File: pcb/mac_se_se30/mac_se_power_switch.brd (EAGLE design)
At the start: 27.1 x 59 mm, 7 parts, among them J1 POWER_JACKPTH

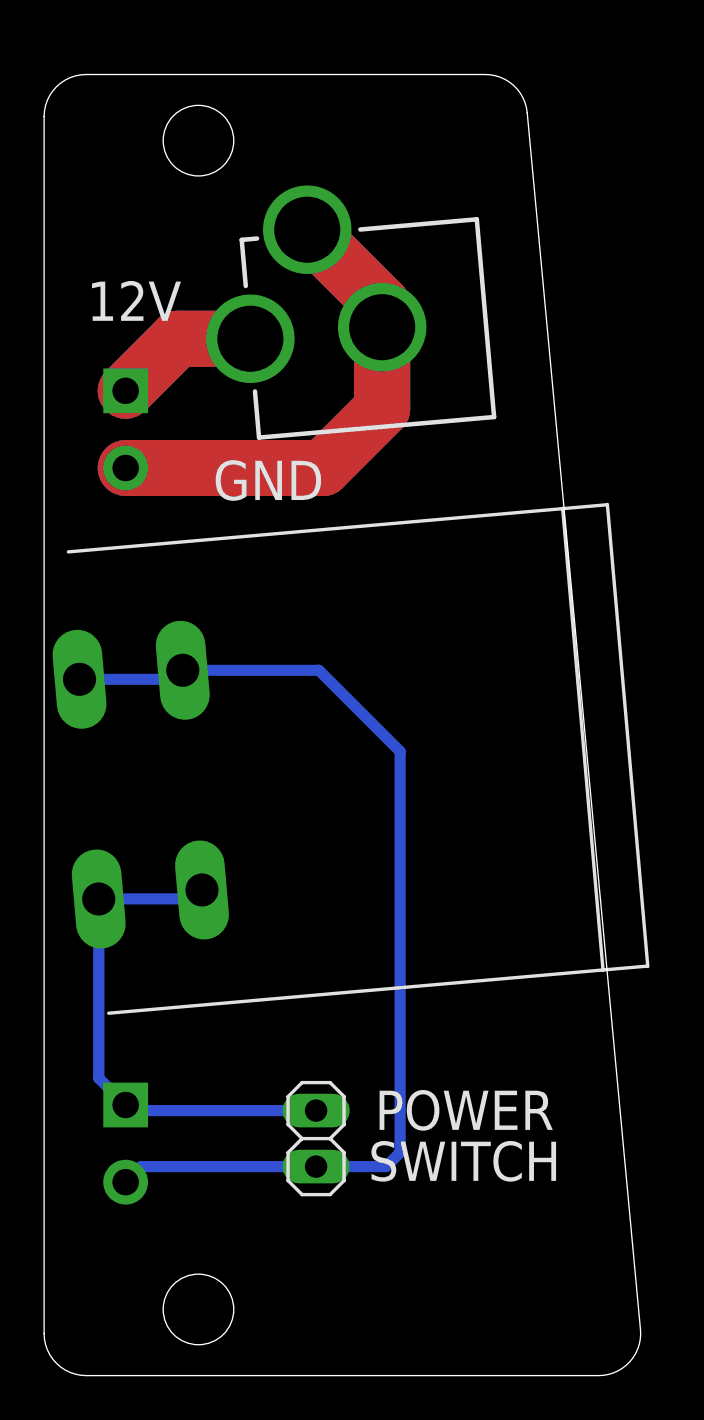
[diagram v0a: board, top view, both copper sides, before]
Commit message: updating mac SE atx adaptor
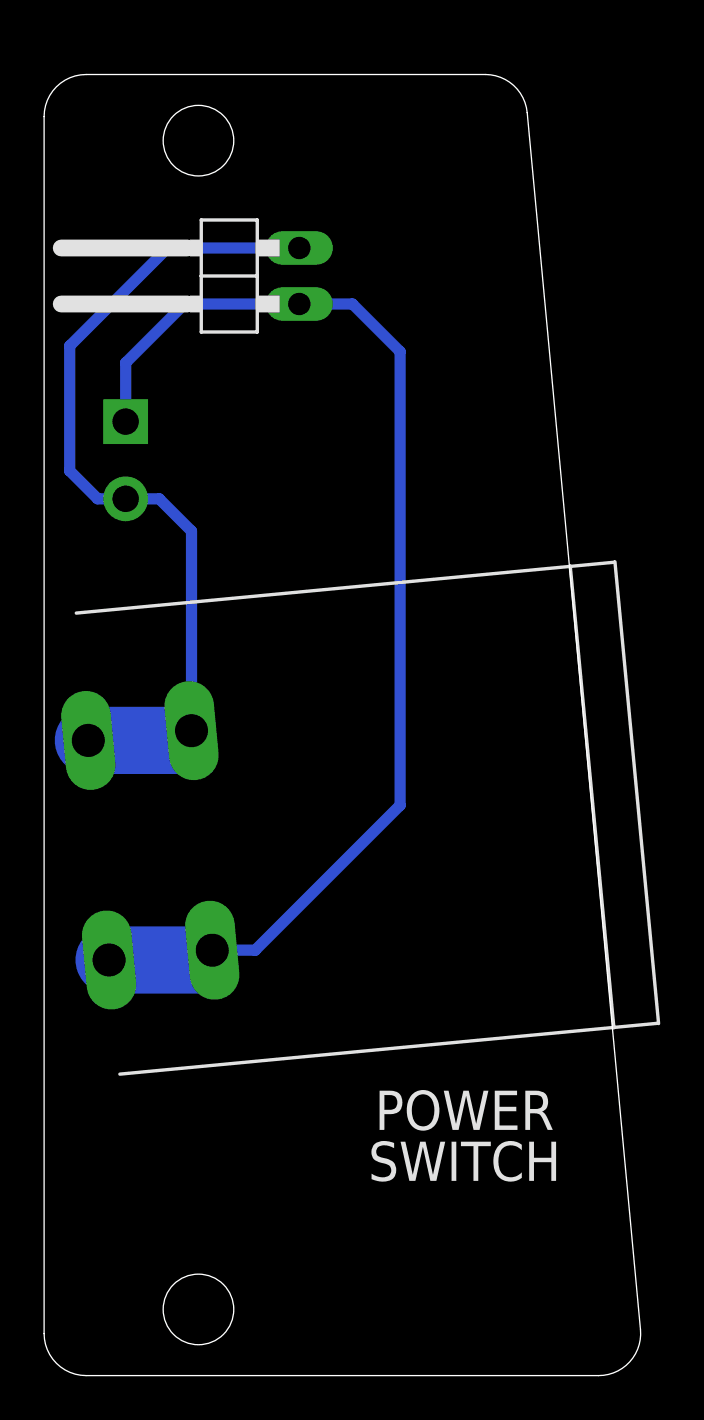
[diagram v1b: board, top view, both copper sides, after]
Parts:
- removed J1: POWER_JACKPTH, SparkFun:POWER_JACK_PTH
- removed J2: (no value), atx_power_control:SCREWTERMINAL-3.5MM-2-NS
- JP2: device pinhead:1X02 -> pinhead:1X02/90
- moved JP2 39.4 mm to (0.76, 46.9), turned to 90 degrees
- moved J7 31.0 mm to (-3.30, 40.3)
- moved U$1 2.80 mm to (-4.55, 21.1), turned to 275.4 degrees
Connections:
- removed net N$1: J1.GND, J1.GNDBREAK, J2.2
- removed net N$4: J1.PWR, J2.1
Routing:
- net N$1: track 44.5 -> 0.00 mm
- net N$3: track 23.4 -> 53.8 mm
- net N$4: track 13.3 -> 0.00 mm
- net N$2: track 47.4 -> 38.5 mm
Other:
- board text added: "PT1 dekuNukem Nov 2022"
- board text removed: "12V"
- board text removed: "GND"
- board text removed: "PT0 dekuNukem Nov 2022"
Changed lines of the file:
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@@
 <wire x1="20.0442375" y1="-0.918428125" x2="14.906890625" y2="54.27156875" width="0" layer="20"/>
 <wire x1="14.906890625" y1="54.27156875" x2="13.010090625" y2="56" width="0" layer="20" curve="84.681981"/>
-<text x="10.541" y="1.397" size="1.778" layer="26" distance="35" rot="MR180" align="center">Instructions:
+<text x="11.303" y="0.635" size="1.778" layer="26" distance="35" rot="MR180" align="center">Instructions:
 atx4vc.com</text>
 <text x="10.541" y="25.273" size="1.778" layer="26" distance="35" rot="MR90" align="center">Macintosh SE ATX
 Power Board</text>
-<text x="4.318" y="24.765" size="1.4224" layer="26" distance="30" rot="MR90" align="center">PT0 dekuNukem
+<text x="4.318" y="24.765" size="1.4224" layer="26" distance="30" rot="MR90" align="center">PT1 dekuNukem
 Nov 2022</text>
 <wire x1="14.7334" y1="56.8706" x2="20.3722" y2="-3.8862" width="0.1524" layer="51"/>
-<text x="3.175" y="37.592" size="1.778" layer="25" distance="30" rot="R180" align="center">GND</text>
-<text x="-2.921" y="45.72" size="1.778" layer="25" distance="30" rot="R180" align="center">12V</text>
 <text x="12.065" y="7.874" size="1.778" layer="25" distance="30" rot="R180" align="center">POWER
 SWITCH</text>
@@
 </autorouter>
 <elements>
-<element name="J7" library="atx_power_control" package="SCREWTERMINAL-3.5MM-2-NS" value="" x="-3.302" y="9.271" smashed="yes" rot="R270">
-<attribute name="PROD_ID" value="CONN-13512" x="-3.302" y="9.271" size="1.778" layer="27" rot="R270" display="off"/>
-<attribute name="SF_ID" value="PRT-09918" x="-3.302" y="9.271" size="1.778" layer="27" rot="R270" display="off"/>
-<attribute name="SF_SKU" value="PRT-08432" x="-3.302" y="9.271" size="1.778" layer="27" rot="R270" display="off"/>
-<attribute name="SKU" value="PRT-09914" x="-3.302" y="9.271" size="1.778" layer="27" rot="R270" display="off"/>
-<attribute name="VALUE" x="-2.032" y="10.541" size="0.6096" layer="27" font="vector" ratio="20" rot="R270"/>
+<element name="J7" library="atx_power_control" package="SCREWTERMINAL-3.5MM-2-NS" value="" x="-3.302" y="40.259" smashed="yes" rot="R270">
+<attribute name="PROD_ID" value="CONN-13512" x="-3.302" y="40.259" size="1.778" layer="27" rot="R270" display="off"/>
+<attribute name="SF_ID" value="PRT-09918" x="-3.302" y="40.259" size="1.778" layer="27" rot="R270" display="off"/>
+<attribute name="SF_SKU" value="PRT-08432" x="-3.302" y="40.259" size="1.778" layer="27" rot="R270" display="off"/>
+<attribute name="SKU" value="PRT-09914" x="-3.302" y="40.259" size="1.778" layer="27" rot="R270" display="off"/>
+<attribute name="VALUE" x="-2.032" y="41.529" size="0.6096" layer="27" font="vector" ratio="20" rot="R270"/>
 </element>
-<element name="JP2" library="pinhead" library_urn="urn:adsk.eagle:library:325" package="1X02" package3d_urn="urn:adsk.eagle:package:22435/2" value="" x="5.334" y="7.747" smashed="yes" rot="R270">
-<attribute name="POPULARITY" value="98" x="5.334" y="7.747" size="1.778" layer="27" rot="R270" display="off"/>
-<attribute name="VALUE" x="2.159" y="10.287" size="1.27" layer="27" rot="R270"/>
+<element name="JP2" library="pinhead" library_urn="urn:adsk.eagle:library:325" package="1X02/90" package3d_urn="urn:adsk.eagle:package:22437/2" value="" x="0.762" y="46.863" smashed="yes" rot="R90">
+<attribute name="POPULARITY" value="24" x="0.762" y="46.863" size="1.778" layer="27" rot="R90" display="off"/>
+<attribute name="VALUE" x="3.937" y="44.323" size="1.27" layer="27" rot="R90"/>
 </element>
 <element name="U$2" library="a" package="M3_MOUNTING_HOLE_PACK" value="M3_MOUNTING_HOLE" x="0" y="0" smashed="yes"/>
 <element name="U$3" library="a" package="M3_MOUNTING_HOLE_PACK" value="M3_MOUNTING_HOLE" x="0" y="53" smashed="yes"/>
-<element name="U$1" library="atx4vc" package="ROCK_SWITCH" value="ROCK_SW" x="-4.984" y="23.892" smashed="yes" rot="R275"/>
-<element name="J1" library="SparkFun" package="POWER_JACK_PTH" value="POWER_JACKPTH" x="16.002" y="45.212" smashed="yes" rot="R95"/>
-<element name="J2" library="atx_power_control" package="SCREWTERMINAL-3.5MM-2-NS" value="" x="-3.302" y="41.656" smashed="yes" rot="R270">
-<attribute name="PROD_ID" value="CONN-13512" x="-3.302" y="41.656" size="1.778" layer="27" rot="R270" display="off"/>
-<attribute name="SF_ID" value="PRT-09918" x="-3.302" y="41.656" size="1.778" layer="27" rot="R270" display="off"/>
-<attribute name="SF_SKU" value="PRT-08432" x="-3.302" y="41.656" size="1.778" layer="27" rot="R270" display="off"/>
-<attribute name="SKU" value="PRT-09914" x="-3.302" y="41.656" size="1.778" layer="27" rot="R270" display="off"/>
-<attribute name="VALUE" x="-2.032" y="42.926" size="0.6096" layer="27" font="vector" ratio="20" rot="R270"/>
-</element>
+<element name="U$1" library="atx4vc" package="ROCK_SWITCH" value="ROCK_SW" x="-4.5522" y="21.1234" smashed="yes" rot="R275.4"/>
 </elements>
 <signals>
@@
 <contactref element="J7" pad="2"/>
 <contactref element="JP2" pad="2"/>
-<wire x1="-5.39363125" y1="28.5741125" x2="-1.12115" y2="28.5741125" width="0.508" layer="16"/>
-<wire x1="-1.12115" y1="28.5741125" x2="-0.711515625" y2="28.983746875" width="0.508" layer="16"/>
-<wire x1="-0.711515625" y1="28.983746875" x2="5.460253125" y2="28.983746875" width="0.508" layer="16"/>
-<wire x1="8.509" y1="6.477" x2="5.334" y2="6.477" width="0.508" layer="16"/>
-<wire x1="9.144" y1="7.112" x2="8.509" y2="6.477" width="0.508" layer="16"/>
-<wire x1="9.144" y1="25.3" x2="9.144" y2="7.112" width="0.508" layer="16"/>
-<wire x1="5.460253125" y1="28.983746875" x2="9.144" y2="25.3" width="0.508" layer="16"/>
-<wire x1="-3.302" y1="5.771" x2="-2.596" y2="6.477" width="0.508" layer="16"/>
-<wire x1="-2.596" y1="6.477" x2="5.334" y2="6.477" width="0.508" layer="16"/>
+<wire x1="-4.99450625" y1="25.802540625" x2="-0.68935" y2="25.8055125" width="3.048" layer="16"/>
+<wire x1="-0.68935" y1="25.8055125" x2="-0.315365625" y2="26.24485" width="0.508" layer="16"/>
+<wire x1="-0.315365625" y1="35.296365625" x2="-1.778" y2="36.759" width="0.508" layer="16"/>
+<wire x1="-3.302" y1="36.759" x2="-1.778" y2="36.759" width="0.508" layer="16"/>
+<wire x1="-0.315365625" y1="35.296365625" x2="-0.315365625" y2="26.24485" width="0.508" layer="16"/>
+<wire x1="-3.302" y1="36.759" x2="-4.572" y2="36.759" width="0.508" layer="16"/>
+<wire x1="-4.572" y1="36.759" x2="-5.842" y2="38.029" width="0.508" layer="16"/>
+<wire x1="-5.842" y1="38.029" x2="-5.842" y2="43.688" width="0.508" layer="16"/>
+<wire x1="-5.842" y1="43.688" x2="-1.397" y2="48.133" width="0.508" layer="16"/>
+<wire x1="-1.397" y1="48.133" x2="4.572" y2="48.133" width="0.508" layer="16"/>
 </signal>
 <signal name="N$3">
@@
 <contactref element="J7" pad="1"/>
 <contactref element="JP2" pad="1"/>
-<wire x1="5.334" y1="9.017" x2="-3.048" y2="9.017" width="0.508" layer="16"/>
-<wire x1="-3.048" y1="9.017" x2="-3.302" y2="9.271" width="0.508" layer="16"/>
-<wire x1="-3.302" y1="9.271" x2="-4.522071875" y2="10.491071875" width="0.508" layer="16"/>
-<wire x1="-4.522071875" y1="10.491071875" x2="-4.522071875" y2="18.612165625" width="0.508" layer="16"/>
-<wire x1="-4.522071875" y1="18.612165625" x2="-0.249596875" y2="18.612165625" width="0.508" layer="16"/>
-<wire x1="-0.249596875" y1="18.612165625" x2="0.1600375" y2="19.0218" width="0.508" layer="16"/>
-</signal>
-<signal name="N$1">
-<contactref element="J1" pad="GNDBREAK"/>
-<contactref element="J1" pad="GND"/>
-<contactref element="J2" pad="2"/>
-<wire x1="4.933084375" y1="48.961546875" x2="8.3313" y2="45.56333125" width="2.54" layer="16"/>
-<wire x1="8.3313" y1="45.56333125" x2="8.3313" y2="44.5409" width="2.54" layer="16"/>
-<wire x1="8.3313" y1="44.5409" x2="8.3313" y2="40.8433" width="2.54" layer="16"/>
-<wire x1="5.644" y1="38.156" x2="-3.302" y2="38.156" width="2.54" layer="16"/>
-<wire x1="8.3313" y1="40.8433" x2="5.644" y2="38.156" width="2.54" layer="16"/>
-<wire x1="4.933084375" y1="48.961546875" x2="8.3313" y2="45.56333125" width="2.54" layer="1"/>
-<wire x1="8.3313" y1="45.56333125" x2="8.3313" y2="44.5409" width="2.54" layer="1"/>
-<wire x1="8.3313" y1="44.5409" x2="8.3313" y2="40.8433" width="2.54" layer="1"/>
-<wire x1="5.644" y1="38.156" x2="-3.302" y2="38.156" width="2.54" layer="1"/>
-<wire x1="8.3313" y1="40.8433" x2="5.644" y2="38.156" width="2.54" layer="1"/>
-</signal>
-<signal name="N$4">
-<contactref element="J1" pad="PWR"/>
-<contactref element="J2" pad="1"/>
-<wire x1="-3.302" y1="41.656" x2="-0.940034375" y2="44.017965625" width="2.54" layer="16"/>
-<wire x1="-0.940034375" y1="44.017965625" x2="2.354134375" y2="44.017965625" width="2.54" layer="16"/>
-<wire x1="2.354134375" y1="44.017965625" x2="-0.940034375" y2="44.017965625" width="2.54" layer="1"/>
-<wire x1="-0.940034375" y1="44.017965625" x2="-3.302" y2="41.656" width="2.54" layer="1"/>
+<wire x1="-4.053425" y1="15.84691875" x2="0.182203125" y2="15.843565625" width="3.048" layer="16"/>
+<wire x1="0.182203125" y1="15.843565625" x2="0.6257125" y2="16.289228125" width="0.508" layer="16"/>
+<wire x1="2.573228125" y1="16.289228125" x2="0.6257125" y2="16.289228125" width="0.508" layer="16"/>
+<wire x1="9.144" y1="22.86" x2="2.573228125" y2="16.289228125" width="0.508" layer="16"/>
+<wire x1="-3.302" y1="40.259" x2="-3.302" y2="42.926" width="0.508" layer="16"/>
+<wire x1="-0.635" y1="45.593" x2="4.572" y2="45.593" width="0.508" layer="16"/>
+<wire x1="-3.302" y1="42.926" x2="-0.635" y2="45.593" width="0.508" layer="16"/>
+<wire x1="4.572" y1="45.593" x2="6.985" y2="45.593" width="0.508" layer="16"/>
+<wire x1="6.985" y1="45.593" x2="9.144" y2="43.434" width="0.508" layer="16"/>
+<wire x1="9.144" y1="43.434" x2="9.144" y2="22.86" width="0.508" layer="16"/>
 </signal>
 </signals>

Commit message: updated mac SE pcb
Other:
- board text added: "Macintosh SE ATX Power Switch"
- board text removed: "Macintosh SE ATX Power Board"
- board text removed: "POWER SWITCH"
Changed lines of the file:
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@@
 <wire x1="20.0442375" y1="-0.918428125" x2="14.906890625" y2="54.27156875" width="0" layer="20"/>
 <wire x1="14.906890625" y1="54.27156875" x2="13.010090625" y2="56" width="0" layer="20" curve="84.681981"/>
-<text x="11.303" y="0.635" size="1.778" layer="26" distance="35" rot="MR180" align="center">Instructions:
+<text x="8.763" y="7.493" size="1.778" layer="25" distance="35" rot="R180" align="center">Instructions:
 atx4vc.com</text>
-<text x="10.541" y="25.273" size="1.778" layer="26" distance="35" rot="MR90" align="center">Macintosh SE ATX
-Power Board</text>
-<text x="4.318" y="24.765" size="1.4224" layer="26" distance="30" rot="MR90" align="center">PT1 dekuNukem
+<text x="11.303" y="44.577" size="1.778" layer="25" distance="35" rot="R270" align="center">Macintosh SE ATX
+Power Switch</text>
+<text x="10.541" y="1.27" size="1.4224" layer="25" distance="30" align="center">PT1 dekuNukem
 Nov 2022</text>
 <wire x1="14.7334" y1="56.8706" x2="20.3722" y2="-3.8862" width="0.1524" layer="51"/>
-<text x="12.065" y="7.874" size="1.778" layer="25" distance="30" rot="R180" align="center">POWER
-SWITCH</text>
 </plain>
 <attributes>

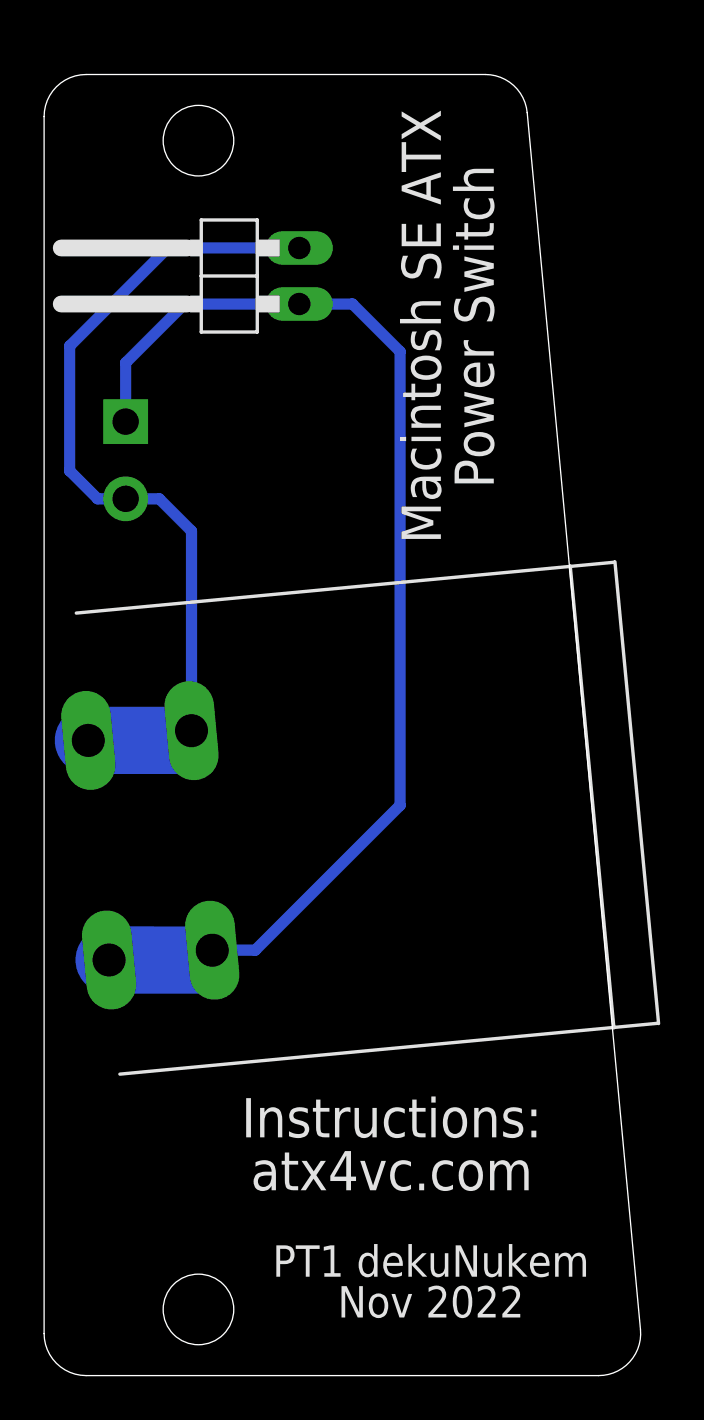
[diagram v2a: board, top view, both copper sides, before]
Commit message: updated switch footprint
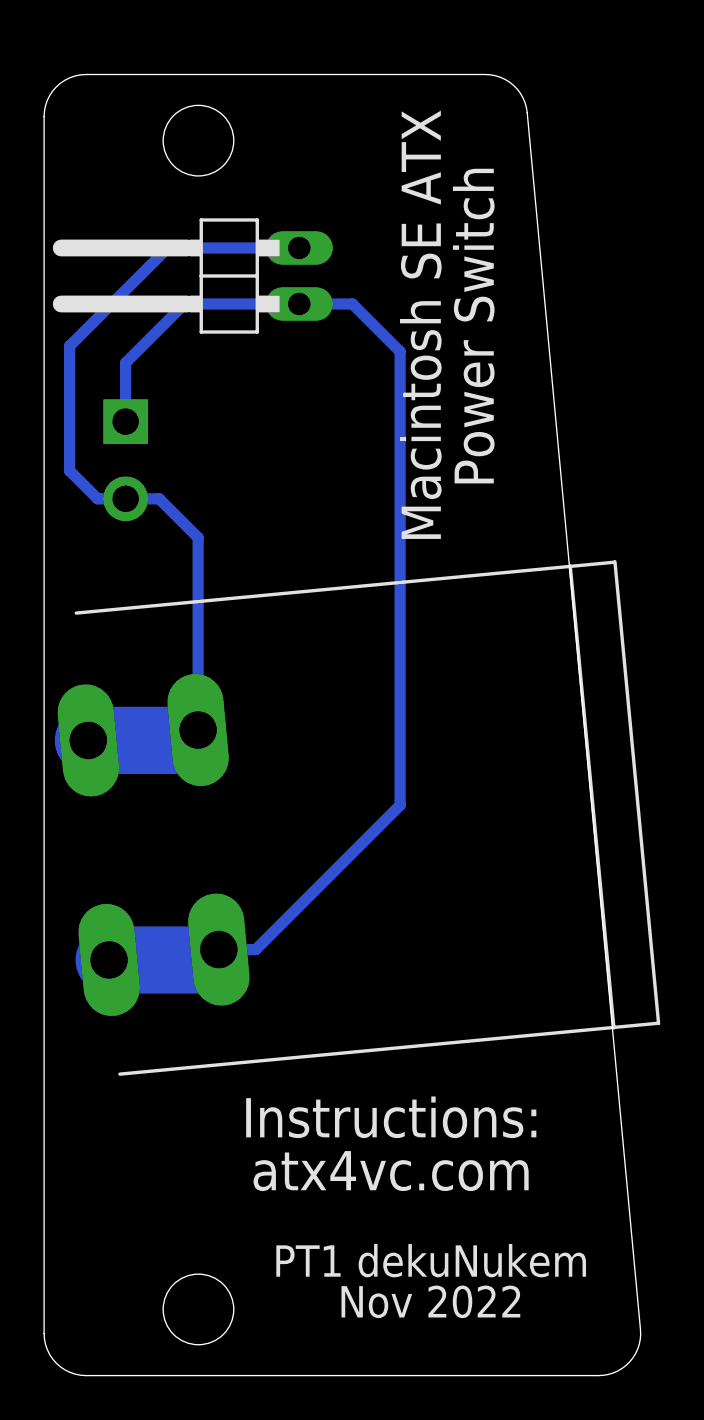
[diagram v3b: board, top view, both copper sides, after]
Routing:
- net N$3: track 53.8 -> 52.9 mm
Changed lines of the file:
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@@
 <contactref element="JP2" pad="2"/>
 <wire x1="-4.99450625" y1="25.802540625" x2="-0.68935" y2="25.8055125" width="3.048" layer="16"/>
-<wire x1="-0.68935" y1="25.8055125" x2="-0.315365625" y2="26.24485" width="0.508" layer="16"/>
-<wire x1="-0.315365625" y1="35.296365625" x2="-1.778" y2="36.759" width="0.508" layer="16"/>
 <wire x1="-3.302" y1="36.759" x2="-1.778" y2="36.759" width="0.508" layer="16"/>
-<wire x1="-0.315365625" y1="35.296365625" x2="-0.315365625" y2="26.24485" width="0.508" layer="16"/>
 <wire x1="-3.302" y1="36.759" x2="-4.572" y2="36.759" width="0.508" layer="16"/>
 <wire x1="-4.572" y1="36.759" x2="-5.842" y2="38.029" width="0.508" layer="16"/>
@@
 <wire x1="-5.842" y1="43.688" x2="-1.397" y2="48.133" width="0.508" layer="16"/>
 <wire x1="-1.397" y1="48.133" x2="4.572" y2="48.133" width="0.508" layer="16"/>
+<wire x1="-0.016696875" y1="34.997696875" x2="-0.016696875" y2="26.27308125" width="0.508" layer="16"/>
+<wire x1="-1.778" y1="36.759" x2="-0.016696875" y2="34.997696875" width="0.508" layer="16"/>
+<wire x1="-0.68935" y1="25.8055125" x2="-0.016696875" y2="26.27308125" width="0" layer="19" extent="16-16"/>
 </signal>
 <signal name="N$3">
@@
 <contactref element="JP2" pad="1"/>
 <wire x1="-4.053425" y1="15.84691875" x2="0.182203125" y2="15.843565625" width="3.048" layer="16"/>
-<wire x1="0.182203125" y1="15.843565625" x2="0.6257125" y2="16.289228125" width="0.508" layer="16"/>
-<wire x1="2.573228125" y1="16.289228125" x2="0.6257125" y2="16.289228125" width="0.508" layer="16"/>
-<wire x1="9.144" y1="22.86" x2="2.573228125" y2="16.289228125" width="0.508" layer="16"/>
 <wire x1="-3.302" y1="40.259" x2="-3.302" y2="42.926" width="0.508" layer="16"/>
 <wire x1="-0.635" y1="45.593" x2="4.572" y2="45.593" width="0.508" layer="16"/>
@@
 <wire x1="4.572" y1="45.593" x2="6.985" y2="45.593" width="0.508" layer="16"/>
 <wire x1="6.985" y1="45.593" x2="9.144" y2="43.434" width="0.508" layer="16"/>
-<wire x1="9.144" y1="43.434" x2="9.144" y2="22.86" width="0.508" layer="16"/>
+<wire x1="9.144" y1="22.86" x2="9.144" y2="43.434" width="0.508" layer="16"/>
+<wire x1="0.92438125" y1="16.3174625" x2="2.6014625" y2="16.3174625" width="0.508" layer="16"/>
+<wire x1="2.6014625" y1="16.3174625" x2="9.144" y2="22.86" width="0.508" layer="16"/>
+<wire x1="0.182203125" y1="15.843565625" x2="0.92438125" y2="16.3174625" width="0" layer="19" extent="16-16"/>
 </signal>
 </signals>
